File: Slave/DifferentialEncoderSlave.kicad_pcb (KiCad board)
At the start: 4 copper layers, 52.5 x 35.2 mm, 21 parts, among them J1 RJ45_Shielded, U1 SN75C1167, U2 MA730, U3 LDFM33PVR

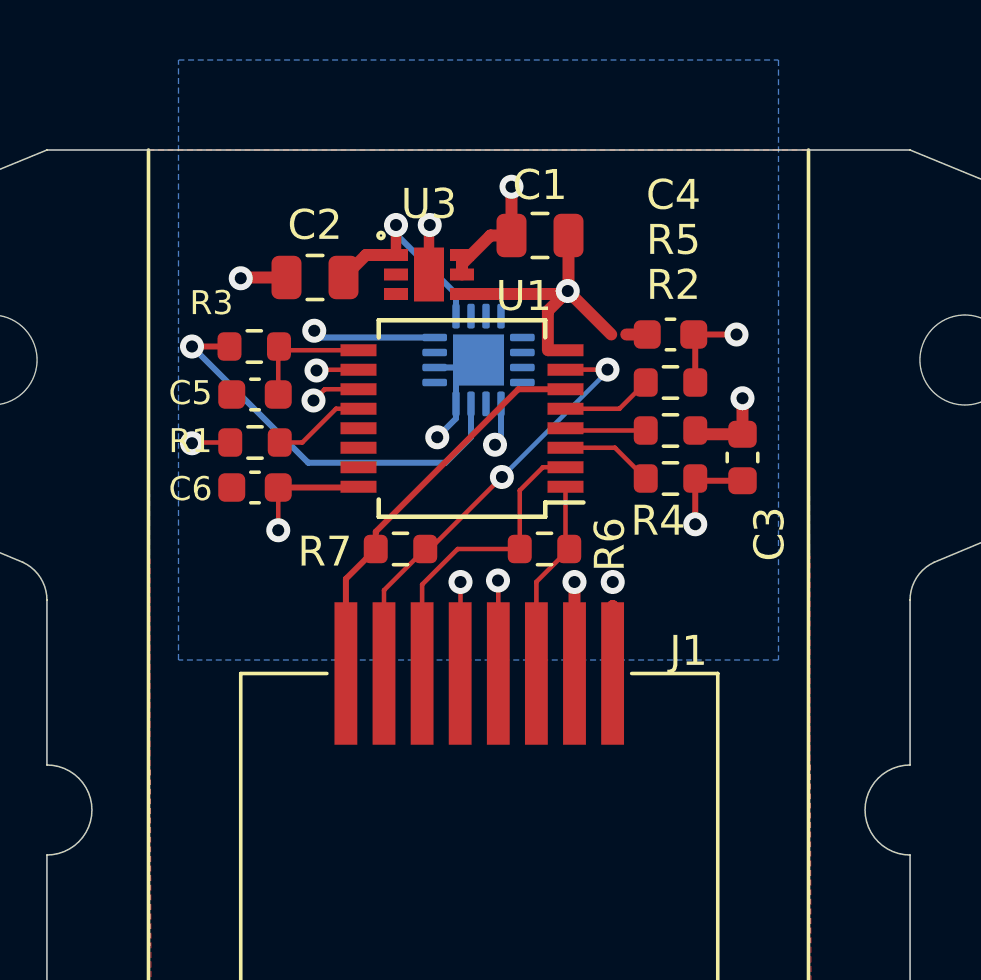
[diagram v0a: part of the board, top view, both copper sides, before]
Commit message: Create AEAT-9922 encoder variant
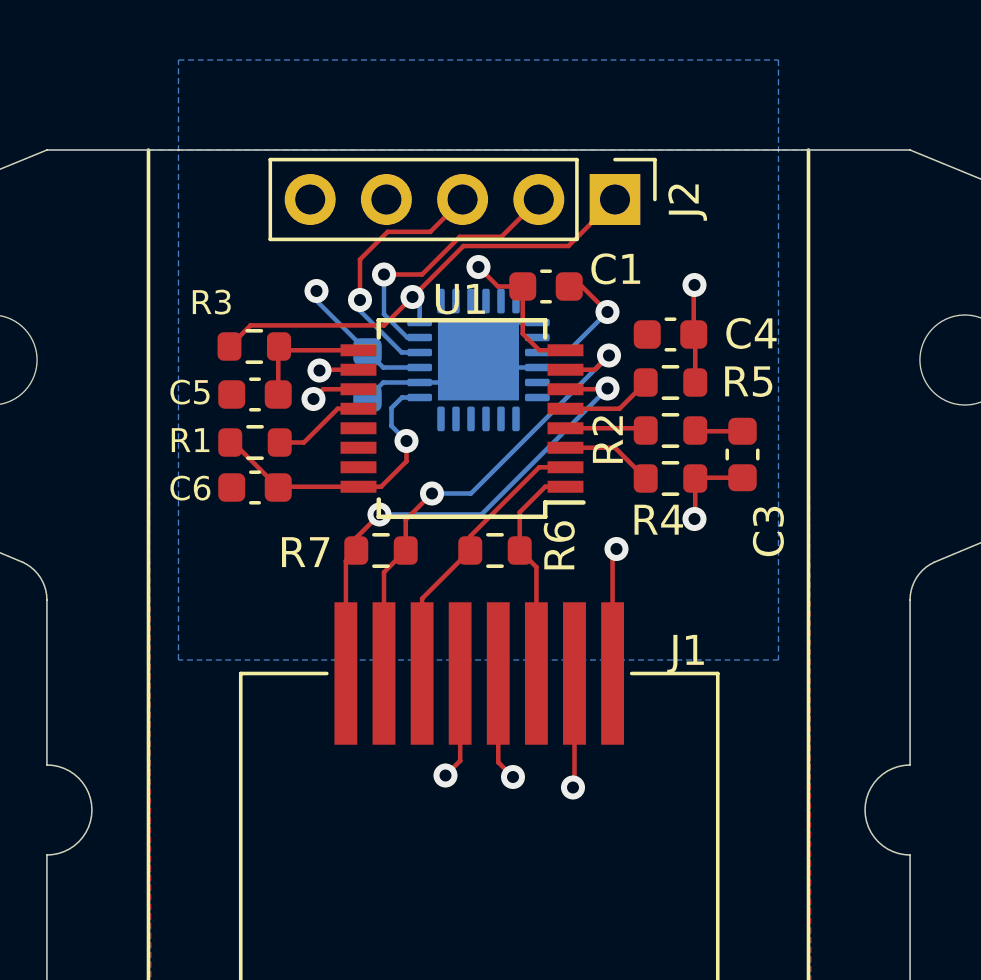
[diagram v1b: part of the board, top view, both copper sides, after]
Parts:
- removed U3: LDFM33PVR, Wetmelon:DFN6-2x2
- added J2: Debug, Connector_PinHeader_2.54mm:PinHeader_1x05_P2.54mm_Vertical, F.Cu at (126.5, 62.6)
- C1: value 1uF -> 100nF; footprint Capacitor_SMD:C_0805_2012Metric -> Capacitor_SMD:C_0603_1608Metric
- C2: value 4.7uF -> 100nF; footprint Capacitor_SMD:C_0805_2012Metric -> Capacitor_SMD:C_0603_1608Metric; moved to B.Cu
- U2: value MA730 -> AEAT-9922; footprint Package_DFN_QFN:QFN-16-1EP_3x3mm_P0.5mm_EP1.7x1.7mm -> Package_DFN_QFN:QFN-24-1EP_4x4mm_P0.5mm_EP2.7x2.7mm
- moved C2 3.69 mm to (118.3, 68.5), turned to 90 degrees
- moved C1 1.71 mm to (124.2, 65.5)
- moved R6 1.65 mm to (122.5, 74.3)
- moved R7 0.65 mm to (118.8, 74.3)
- moved C3 0.10 mm to (130.8, 71.2)
- turned U2 to 90 degrees
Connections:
- C1 pad 1: +5V -> GNDD
- C1 pad 2: GNDD -> +5V
- C2 pad 1: +3V3 -> GNDD
- C2 pad 2: GNDD -> +5V
- U2 pad 10: GNDD -> /CSn
- U2 pad 11: (no net) -> /CLK
- U2 pad 12: /CLK -> /MISO
- U2 pad 13: +3V3 -> (no net)
- U2 pad 17: GNDD -> (no net)
- U2 pad 5: /CSn -> (no net)
- U2 pad 7: /MISO -> +5V
- U2 pad 9: (no net) -> +5V
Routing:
- net +5V: track 14.1 -> 27.0 mm
- net /CSn: track 14.1 -> 24.3 mm
- net /MISO+: track 14.4 -> 21.2 mm
- net +3V3: track 6.63 -> 0.00 mm, vias 1 -> 0
- net /MISO-: track 13.1 -> 19.6 mm
- net GNDD: track 25.3 -> 19.5 mm, vias 6 -> 2
- net /CSn+: track 13.4 -> 16.5 mm, vias 0 -> 2
- net /MISO: track 13.6 -> 15.8 mm
- net /CLK: track 23.9 -> 25.7 mm
- net /CSn-: track 14.7 -> 16.1 mm
- net /CLK+: track 10.5 -> 9.37 mm
- net /CLK-: track 6.73 -> 7.48 mm
